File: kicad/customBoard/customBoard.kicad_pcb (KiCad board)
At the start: 2 copper layers, 78 parts, among them J1 USB4125-GF-A_REVA2, J2 SS-53000-001, J3 FFC3B07-20-T, J4 Micro_SD_Card_Det, J5 ARJM11D7-502-AB-EW2, J6 SS-52100-001, J7 SS-52100-001, J8 SS-52100-001, J9 FFC3B07-20-T, Q1 MMUN2133LT1G, U1 TPS61090RSAR, U2 MCP73871-2CCI_ML, U3 74LVC1G07, U4 RT9742VGJ5, U5 RT9742ENGJ5, U6 TPD4EUSB30, U7 TPD4EUSB30, U8 USB2504A-JT, U9 AP22653W6-7, Y1 24MHz

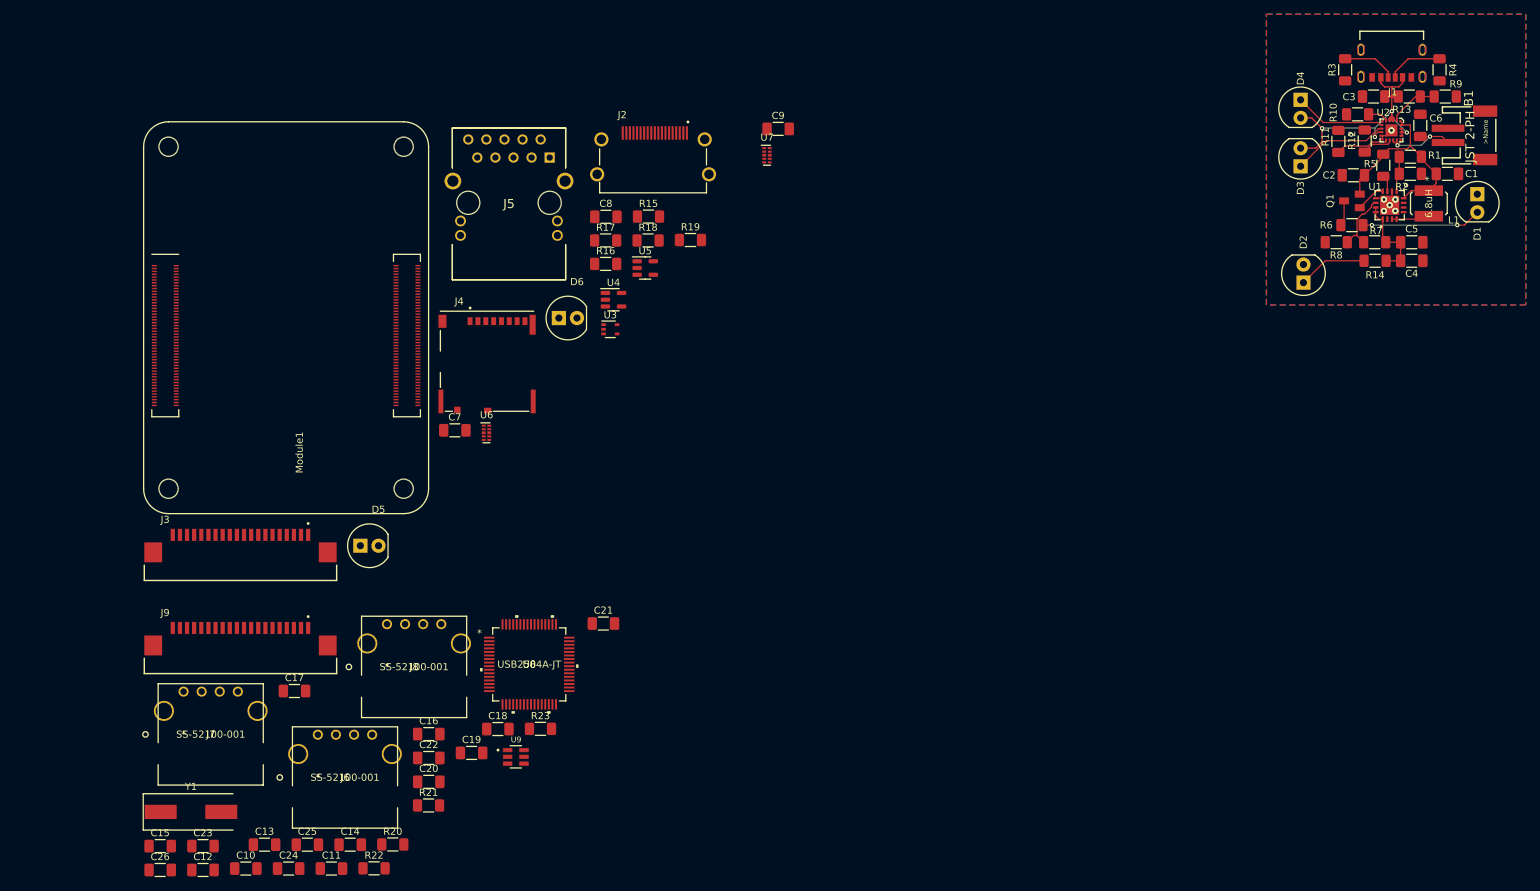
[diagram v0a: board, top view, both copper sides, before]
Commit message: Rework Power PCB and draft SD
Moving things around so they would make sense on the final board. Flipped around some of the power circuit so the battery can be plugged in on the left side to make room for all the ports on the right.
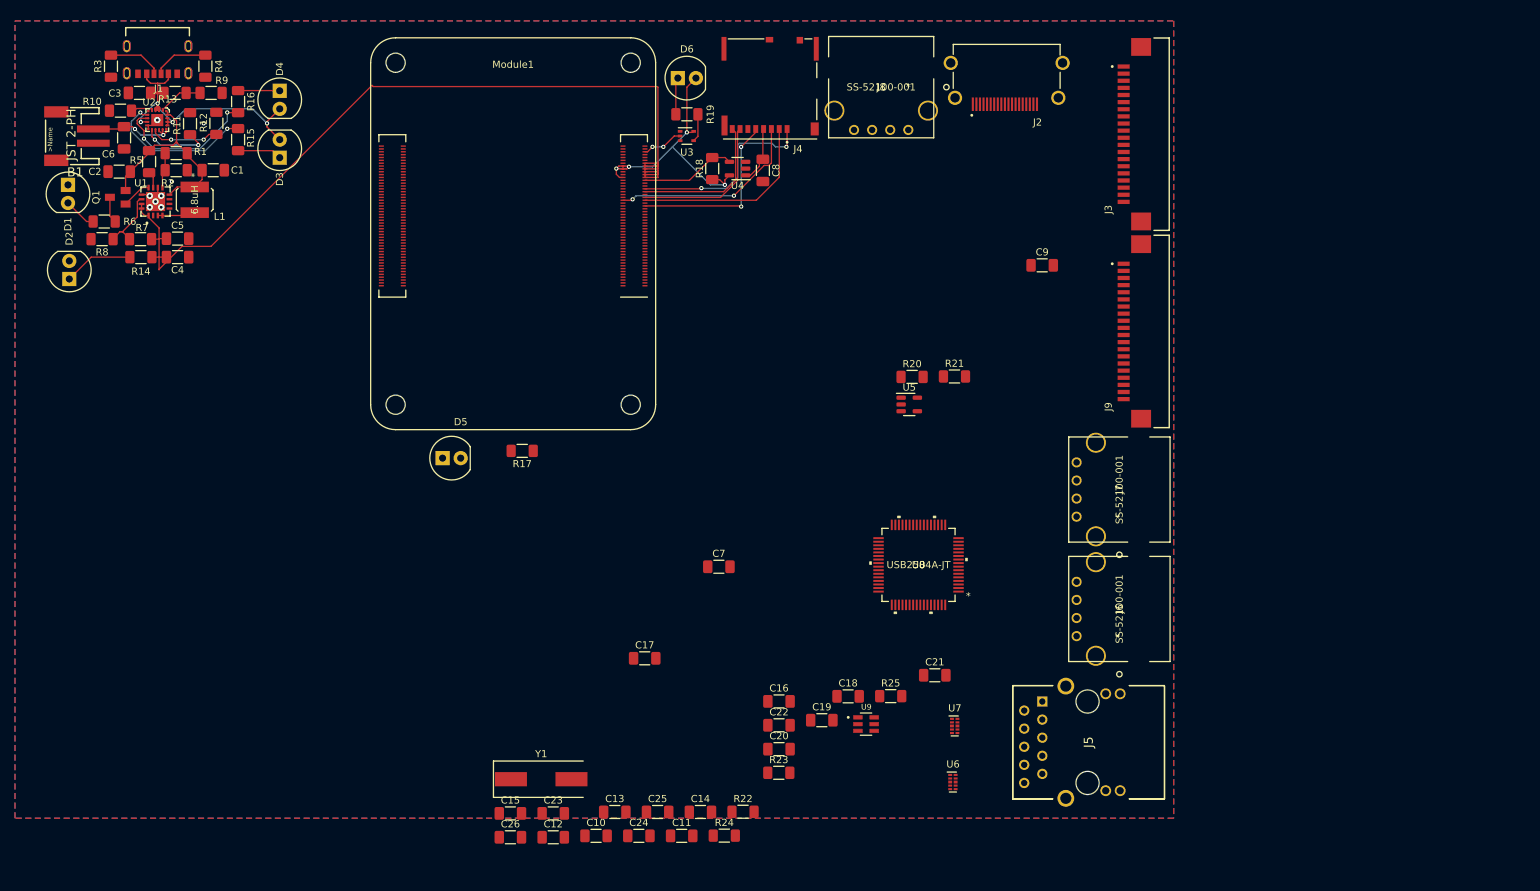
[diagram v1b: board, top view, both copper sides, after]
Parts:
- added R15: 1K, Resistor_SMD:R_1206_3216Metric_Pad1.30x1.75mm_HandSolder, F.Cu at (54.9, 34.8)
- added R16: 1K, Resistor_SMD:R_1206_3216Metric_Pad1.30x1.75mm_HandSolder, F.Cu at (54.9, 29.5)
- moved D1 197.8 mm to (31.0, 43.7)
- moved B1 197.6 mm to (30.8, 34.3), turned to 90 degrees
- moved C6 181.9 mm to (38.9, 34.5), turned to -90 degrees
- moved R6 175.1 mm to (36.1, 46.3), turned to 180 degrees
- moved R10 173.6 mm to (38.4, 30.7)
- moved U2 173.2 mm to (43.5, 32.1)
- moved C1 173.2 mm to (51.4, 39.1)
- moved C2 173.2 mm to (38.2, 39.3)
- moved C3 173.2 mm to (41.0, 28.2)
- moved C4 173.2 mm to (46.4, 51.3)
- moved C5 173.2 mm to (46.4, 48.7)
- moved D2 173.2 mm to (31.2, 51.8)
- moved L1 173.2 mm to (48.8, 43.2)
- moved R1 173.2 mm to (46.2, 36.7)
- moved R13 173.2 mm to (46.0, 28.2)
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- renumbered D4 to D3, D3 to D4, R15 to R17, R16 to R18, R17 to R19, R18 to R20, R19 to R21, R20 to R22, R21 to R23, R22 to R24, R23 to R25
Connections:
- C10 pad 1: /CM4/3.3v -> +3V3
- C11 pad 1: /CM4/3.3v -> +3V3
- C12 pad 1: /CM4/3.3v -> +3V3
- C13 pad 1: /CM4/3.3v -> +3V3
- C14 pad 1: /CM4/3.3v -> +3V3
- C15 pad 1: /CM4/3.3v -> +3V3
- C16 pad 1: /CM4/3.3v -> +3V3
- C17 pad 1: /CM4/3.3v -> +3V3
- C18 pad 2: /CM4/3.3v -> +3V3
- C19 pad 2: /CM4/3.3v -> +3V3
- D3 pad 1: Net-(D4-Pad1) -> Net-(D3-Pad1)
- D4 pad 1: Net-(D3-Pad1) -> Net-(D4-Pad1)
- J2 pad 1: /CM4/HDMI1_D2_P -> /CM4/HDMI0_D2_P
- J2 pad 10: /CM4/HDMI1_CK_P -> /CM4/HDMI0_CK_P
- J2 pad 12: /CM4/HDMI1_CK_N -> /CM4/HDMI0_CK_N
- J2 pad 13: /CM4/HDMI1_CEC -> /CM4/HDMI0_CEC
- J2 pad 15: /CM4/HDMI1_SCL -> /CM4/HDMI0_SCL
- J2 pad 16: /CM4/HDMI1_SDA -> /CM4/HDMI0_SDA
- J2 pad 19: /CM4/HDMI1_HOTPLUG -> /CM4/HDMI0_HOTPLUG
- J2 pad 3: /CM4/HDMI1_D2_N -> /CM4/HDMI0_D2_N
- J2 pad 4: /CM4/HDMI1_D1_P -> /CM4/HDMI0_D1_P
- J2 pad 6: /CM4/HDMI1_D1_N -> /CM4/HDMI0_D1_N
- J2 pad 7: /CM4/HDMI1_D0_P -> /CM4/HDMI0_D0_P
- J2 pad 9: /CM4/HDMI1_D0_N -> /CM4/HDMI0_D0_N
- J3 pad 1: /CM4/HDMI0_D2_P -> /CM4/HDMI1_D2_P
- J3 pad 10: /CM4/HDMI0_CK_P -> /CM4/HDMI1_CK_P
- J3 pad 12: /CM4/HDMI0_CK_N -> /CM4/HDMI1_CK_N
- J3 pad 13: /CM4/HDMI0_CEC -> /CM4/HDMI1_CEC
- J3 pad 15: /CM4/HDMI0_SCL -> /CM4/HDMI1_SCL
- J3 pad 16: /CM4/HDMI0_SDA -> /CM4/HDMI1_SDA
- J3 pad 19: /CM4/HDMI0_HOTPLUG -> /CM4/HDMI1_HOTPLUG
- J3 pad 3: /CM4/HDMI0_D2_N -> /CM4/HDMI1_D2_N
- J3 pad 4: /CM4/HDMI0_D1_P -> /CM4/HDMI1_D1_P
- J3 pad 6: /CM4/HDMI0_D1_N -> /CM4/HDMI1_D1_N
- J3 pad 7: /CM4/HDMI0_D0_P -> /CM4/HDMI1_D0_P
- J3 pad 9: /CM4/HDMI0_D0_N -> /CM4/HDMI1_D0_N
- J8 pad 2: GND -> /USB/D4_N
- J8 pad 3: GND -> /USB/D4_P
- Module1 pad 86: /CM4/3.3v -> +3V3
- U2 pad 7: Net-(D4-Pad1) -> Net-(R15-Pad2)
- U2 pad 8: Net-(D3-Pad1) -> Net-(R16-Pad2)
- U8 pad 1: /CM4/3.3v -> +3V3
- U8 pad 13: /CM4/3.3v -> +3V3
- U8 pad 14: GND -> /USB/D4_N
- U8 pad 15: GND -> /USB/D4_P
- U8 pad 28: /CM4/3.3v -> +3V3
- U8 pad 51: /CM4/3.3v -> +3V3
- U8 pad 52: /CM4/3.3v -> +3V3
- U8 pad 61: /CM4/3.3v -> +3V3
- U8 pad 62: /CM4/3.3v -> +3V3
- U8 pad 7: /CM4/3.3v -> +3V3
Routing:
- net /CM4/5v: track 12.5 -> 122.1 mm
- net +3V3: track 0.00 -> 40.6 mm, vias 0 -> 4
- net /CM4/SD_DAT2: track 0.00 -> 27.9 mm, vias 0 -> 2
- net /CM4/SD_CMD: track 0.00 -> 27.8 mm, vias 0 -> 2
- net /CM4/SD_DAT3: track 0.00 -> 27.0 mm
- net /CM4/SD_CLK: track 0.00 -> 25.3 mm, vias 0 -> 2
- net Net-(R15-Pad2): track 0.00 -> 21.6 mm, vias 0 -> 2
- net /CM4/SD_DAT0: track 0.00 -> 21.3 mm
- net Net-(R16-Pad2): track 0.00 -> 21.1 mm, vias 0 -> 2
- net /CM4/SD_DAT1: track 0.00 -> 20.7 mm
- net Net-(Module1-Pad75): track 0.00 -> 13.4 mm
- net Net-(D1-Pad2): track 16.8 -> 4.61 mm, vias 2 -> 0
- net Net-(C8-Pad1): track 0.00 -> 7.93 mm
- net Net-(D3-Pad1): track 13.5 -> 6.25 mm
- net Net-(D4-Pad1): track 12.7 -> 5.85 mm
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
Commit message: Save progress on USB
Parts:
- removed the C12 at (99.1, 132.7)
- removed the C13 at (107.7, 129.2)
- removed the C14 at (119.8, 129.2)
- moved C20 106.8 mm to (151.0, 36.0)
- moved C22 85.7 mm to (174.7, 68.9), turned to -90 degrees
- moved C12 83.0 mm to (162.2, 83.5), turned to 90 degrees
- moved C10 73.7 mm to (156.3, 79.5)
- moved C21 72.7 mm to (169.7, 89.5), turned to -90 degrees
- moved C23 69.0 mm to (146.8, 89.3), turned to 90 degrees
- moved C9 68.3 mm to (159.2, 120.2), turned to 180 degrees
- moved Y1 60.9 mm to (155.4, 106.2)
- moved R21 59.1 mm to (159.2, 127.0)
- moved R22 52.6 mm to (148.1, 81.5), turned to 180 degrees
- moved C14 52.1 mm to (163.3, 99.2), turned to -90 degrees
- moved C7 51.6 mm to (159.3, 58.7)
- moved R24 48.8 mm to (164.1, 105.8), turned to -90 degrees
- moved R20 46.8 mm to (159.3, 113.9)
- moved C11 46.1 mm to (149.0, 99.2), turned to -90 degrees
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- renumbered C15 to C12, C16 to C13, C17 to C14, C18 to C15, C19 to C16, C20 to C17, C21 to C18, C22 to C19, C23 to C20, C24 to C21, C25 to C22, C26 to C23
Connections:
- Module1 pad 103: /CM4/USB2_N -> unconnected-(Module1-Pad103)
- Module1 pad 105: /CM4/USB2_P -> unconnected-(Module1-Pad105)
- Module1 pad 107: GND -> unconnected-(Module1-Pad107)
- Module1 pad 108: GND -> unconnected-(Module1-Pad108)
- Module1 pad 113: GND -> unconnected-(Module1-Pad113)
- Module1 pad 114: GND -> unconnected-(Module1-Pad114)
- Module1 pad 119: GND -> unconnected-(Module1-Pad119)
- Module1 pad 120: GND -> unconnected-(Module1-Pad120)
- Module1 pad 125: GND -> unconnected-(Module1-Pad125)
- Module1 pad 126: GND -> unconnected-(Module1-Pad126)
- Module1 pad 131: GND -> unconnected-(Module1-Pad131)
- Module1 pad 132: GND -> unconnected-(Module1-Pad132)
- Module1 pad 137: GND -> unconnected-(Module1-Pad137)
- Module1 pad 138: GND -> unconnected-(Module1-Pad138)
- Module1 pad 143: /CM4/HDMI1_HOTPLUG -> unconnected-(Module1-Pad143)
- Module1 pad 144: GND -> unconnected-(Module1-Pad144)
- Module1 pad 145: /CM4/HDMI1_SDA -> unconnected-(Module1-Pad145)
- Module1 pad 146: /CM4/HDMI1_D2_P -> unconnected-(Module1-Pad146)
- Module1 pad 147: /CM4/HDMI1_SCL -> unconnected-(Module1-Pad147)
- Module1 pad 148: /CM4/HDMI1_D2_N -> unconnected-(Module1-Pad148)
- Module1 pad 149: /CM4/HDMI1_CEC -> unconnected-(Module1-Pad149)
- Module1 pad 150: GND -> unconnected-(Module1-Pad150)
- Module1 pad 151: /CM4/HDMI0_CEC -> unconnected-(Module1-Pad151)
- Module1 pad 152: /CM4/HDMI1_D1_P -> unconnected-(Module1-Pad152)
- Module1 pad 153: /CM4/HDMI0_HOTPLUG -> unconnected-(Module1-Pad153)
- Module1 pad 154: /CM4/HDMI1_D1_N -> unconnected-(Module1-Pad154)
- Module1 pad 155: GND -> unconnected-(Module1-Pad155)
- Module1 pad 156: GND -> unconnected-(Module1-Pad156)
- Module1 pad 158: /CM4/HDMI1_D0_P -> unconnected-(Module1-Pad158)
- Module1 pad 160: /CM4/HDMI1_D0_N -> unconnected-(Module1-Pad160)
- Module1 pad 161: GND -> unconnected-(Module1-Pad161)
- Module1 pad 162: GND -> unconnected-(Module1-Pad162)
- Module1 pad 164: /CM4/HDMI1_CK_P -> unconnected-(Module1-Pad164)
- Module1 pad 166: /CM4/HDMI1_CK_N -> unconnected-(Module1-Pad166)
- Module1 pad 167: GND -> unconnected-(Module1-Pad167)
- Module1 pad 168: GND -> unconnected-(Module1-Pad168)
- Module1 pad 170: /CM4/HDMI0_D2_P -> unconnected-(Module1-Pad170)
- Module1 pad 172: /CM4/HDMI0_D2_N -> unconnected-(Module1-Pad172)
- Module1 pad 173: GND -> unconnected-(Module1-Pad173)
- Module1 pad 174: GND -> unconnected-(Module1-Pad174)
- Module1 pad 176: /CM4/HDMI0_D1_P -> unconnected-(Module1-Pad176)
- Module1 pad 178: /CM4/HDMI0_D1_N -> unconnected-(Module1-Pad178)
- Module1 pad 179: GND -> unconnected-(Module1-Pad179)
- Module1 pad 180: GND -> unconnected-(Module1-Pad180)
- Module1 pad 182: /CM4/HDMI0_D0_P -> unconnected-(Module1-Pad182)
- Module1 pad 184: /CM4/HDMI0_D0_N -> unconnected-(Module1-Pad184)
- Module1 pad 185: GND -> unconnected-(Module1-Pad185)
- Module1 pad 186: GND -> unconnected-(Module1-Pad186)
- Module1 pad 188: /CM4/HDMI0_CK_P -> unconnected-(Module1-Pad188)
- Module1 pad 190: /CM4/HDMI0_CK_N -> unconnected-(Module1-Pad190)
- Module1 pad 191: GND -> unconnected-(Module1-Pad191)
- Module1 pad 192: GND -> unconnected-(Module1-Pad192)
- Module1 pad 197: GND -> unconnected-(Module1-Pad197)
- Module1 pad 198: GND -> unconnected-(Module1-Pad198)
- Module1 pad 199: /CM4/HDMI0_SDA -> unconnected-(Module1-Pad199)
- Module1 pad 200: /CM4/HDMI0_SCL -> unconnected-(Module1-Pad200)
- U7 pad 1: /CM4/TRD0_P -> /CM4/TRD1_P
- U7 pad 2: /CM4/TRD0_N -> /CM4/TRD1_N
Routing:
- net /CM4/nEXTRST: track 0.00 -> 86.0 mm
- net /USB/VBUS: track 0.00 -> 72.1 mm, vias 0 -> 4
- net +3V3: track 40.6 -> 102.0 mm
- net /USB/D1_N: track 0.00 -> 47.0 mm, vias 0 -> 2
- net /USB/D1_P: track 0.00 -> 46.9 mm, vias 0 -> 2
- net /CM4/5v: track 122.1 -> 98.4 mm
- net Net-(C17-Pad1): track 0.00 -> 16.0 mm
- net /USB/D2_N: track 0.00 -> 15.0 mm
- net /USB/D2_P: track 0.00 -> 14.9 mm
- net Net-(C18-Pad1): track 0.00 -> 14.3 mm
- net /USB/D3_N: track 0.00 -> 13.0 mm
- net /USB/D3_P: track 0.00 -> 13.0 mm
- net /USB/OCS1: track 0.00 -> 11.4 mm
- net Net-(U8-Pad45): track 0.00 -> 10.2 mm
- net Net-(R24-Pad1): track 0.00 -> 9.27 mm
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- added copper zone on F.Cu, net /USB/VBUS
